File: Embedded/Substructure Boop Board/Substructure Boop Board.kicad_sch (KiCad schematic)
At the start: 1 part, among them U5 R FFC

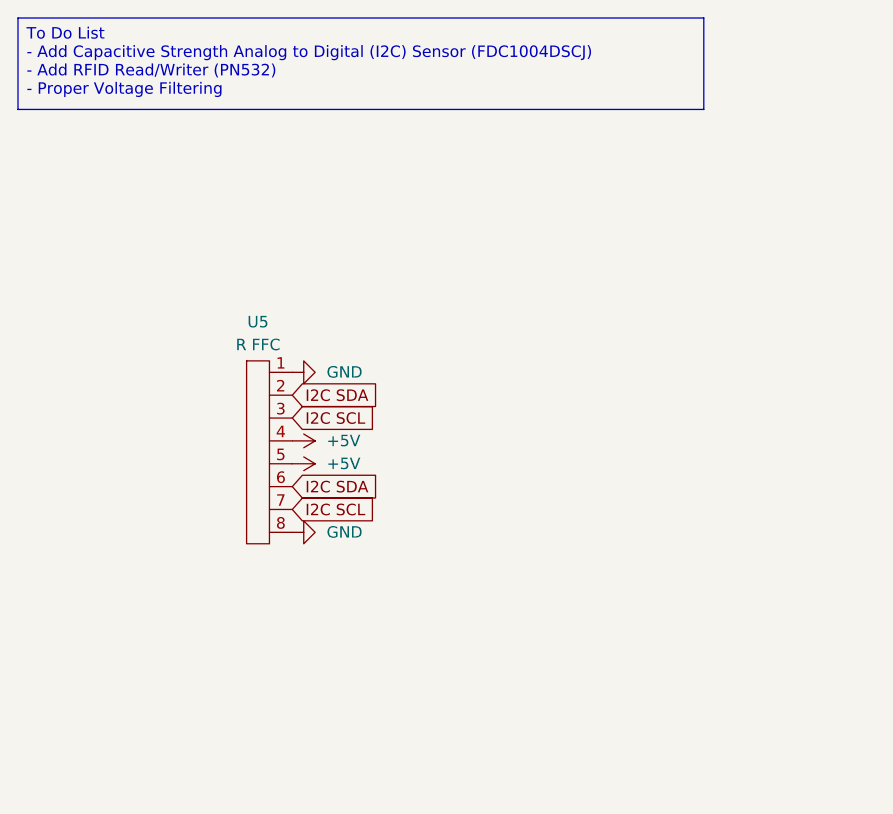
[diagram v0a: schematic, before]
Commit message: Added AD7142ACPZ-500RL7 IC to schematic
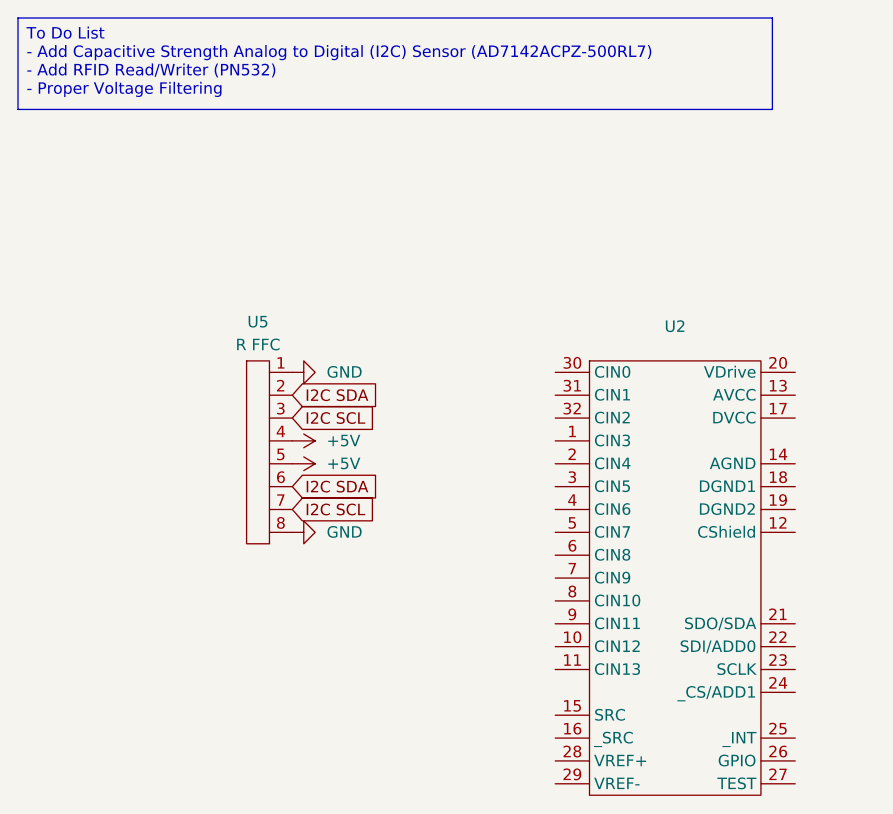
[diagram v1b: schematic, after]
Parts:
- added U2: ~, symbol AD7142ACPZ-500RL7:AD7142ACPZ-500RL7
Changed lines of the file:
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@@
 	(generator_version "9.0")
 	(paper "A4")
-	(text_box "To Do List\n- Add Capacitive Strength Analog to Digital (I2C) Sensor (FDC1004DSCJ)\n- Add RFID Read/Writer (PN532)\n- Proper Voltage Filtering"
+	(text_box "To Do List\n- Add Capacitive Strength Analog to Digital (I2C) Sensor (AD7142ACPZ-500RL7)\n- Add RFID Read/Writer (PN532)\n- Proper Voltage Filtering"
 		(exclude_from_sim no)
 		(at 25.4 25.4 0)
-		(size 76.2 10.16)
+		(size 83.82 10.16)
 		(margins 0.9525 0.9525 0.9525 0.9525)
 		(stroke
@@
 					(unit 1)
 				)
+			)
+		)
+	)
+	(symbol
+		(lib_id "AD7142ACPZ-500RL7:AD7142ACPZ-500RL7")
+		(at 88.9 63.5 0)
+		(unit 1)
+		(exclude_from_sim no)
+		(in_bom yes)
+		(on_board yes)
+		(dnp no)
+		(fields_autoplaced yes)
+		(property "Reference" "U2"
+			(at 98.425 59.69 0)
+			(effects
+				(font
+					(size 1.27 1.27)
+				)
+			)
+		)
+		(property "Value" "~"
+			(at 98.425 62.23 0)
+			(effects
+				(font
+					(size 1.27 1.27)
+				)
+			)
+		)
+		(property "Footprint" ""
+			(at 85.09 64.77 0)
+			(effects
+				(font
+					(size 1.27 1.27)
+				)
+				(hide yes)
+			)
+		)
+		(property "Datasheet" ""
+			(at 85.09 64.77 0)
+			(effects
+				(font
+					(size 1.27 1.27)
+				)
+				(hide yes)
+			)
+		)
+		(property "Description" ""
+			(at 85.09 64.77 0)
+			(effects
+				(font
+					(size 1.27 1.27)
+				)
+				(hide yes)
+			)
+		)
+		(pin "8"
+		)
+		(pin "15"
+		)
+		(pin "1"
+		)
+		(pin "5"
+		)
+		(pin "9"
+		)
+		(pin "11"
+		)
+		(pin "16"
+		)
+		(pin "12"
+		)
+		(pin "25"
+		)
+		(pin "30"
+		)
+		(pin "6"
+		)
+		(pin "14"
+		)
+		(pin "3"
+		)
+		(pin "4"
+		)
+		(pin "10"
+		)
+		(pin "32"
+		)
+		(pin "29"
+		)
+		(pin "19"
+		)
+		(pin "21"
+		)
+		(pin "7"
+		)
+		(pin "2"
+		)
+		(pin "31"
+		)
+		(pin "13"
+		)
+		(pin "28"
+		)
+		(pin "20"
+		)
+		(pin "17"
+		)
+		(pin "18"
+		)
+		(pin "22"
+		)
+		(pin "23"
+		)
+		(pin "24"
+		)
+		(pin "26"
+		)
+		(pin "27"
+		)
+		(instances
+			(project ""
+				(path "/6d158939-39e3-4f58-b43a-760f32d1166c"
+					(reference "U2")
+					(unit 1)
+				)

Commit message: Added Capacitive sensor driving circuitry
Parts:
- added C1: 10nF, Capacitor_SMD:C_0603_1608Metric_Pad1.08x0.95mm_HandSolder, symbol Device:C
- added C2: 10uF, Capacitor_SMD:C_0603_1608Metric_Pad1.08x0.95mm_HandSolder, symbol Device:C
- added C3: 0.1uF, Capacitor_SMD:C_0603_1608Metric_Pad1.08x0.95mm_HandSolder, symbol Device:C
- added R1, R2: 2.2K, Resistor_SMD:R_0603_1608Metric_Pad0.98x0.95mm_HandSolder, symbol Device:R
- U2: value ~ -> AD7142ACPZ-500RL7
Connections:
- net GND: now also U2.14 (AGND), U2.18 (DGND1), U2.19 (DGND2), U2.22 (SDI/ADD0), U2.24 (_CS/ADD1), U2.27 (TEST), U2.29 (VREF-), C1.1, C2.2, C3.2
- net I2C SCL: now also U2.23 (SCLK), R2.1
- net I2C SDA: now also U2.21 (SDO/SDA), R1.2
- net at U2.12 (CShield): now also C1.2
- net +3V3: now reaches U2.13 (AVCC)
- net +3V3: now also U2.17 (DVCC), U2.20 (VDrive), U2.28 (VREF+), C2.1, C3.1, R1.1, R2.2
- no-connect marks 0 -> 3

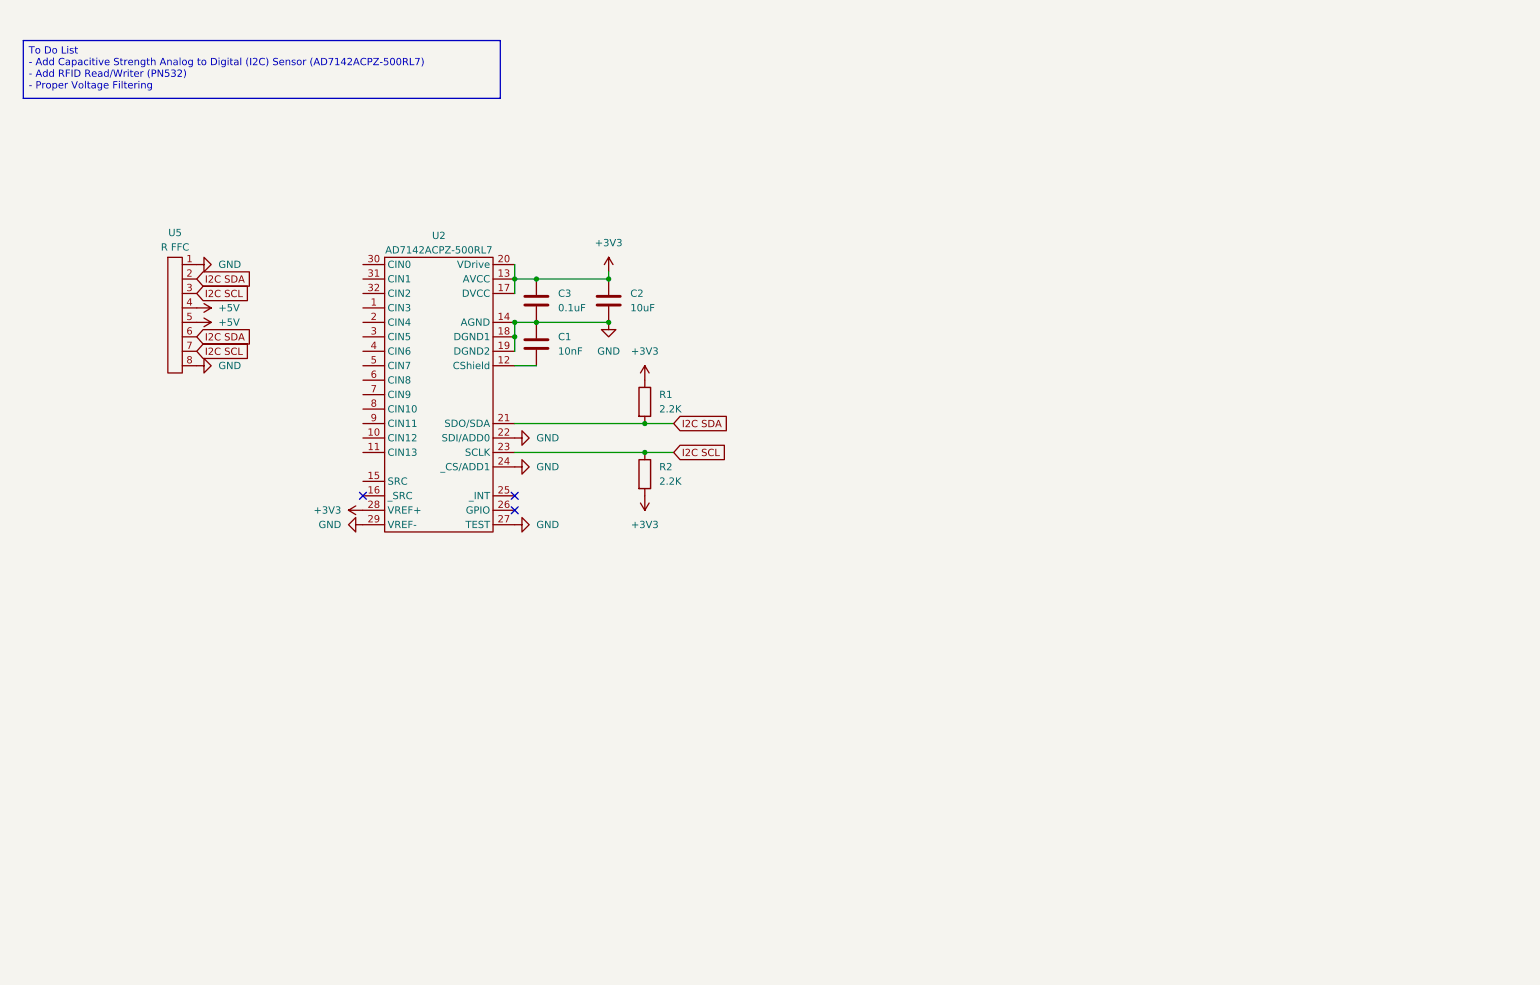
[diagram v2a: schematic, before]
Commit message: Added PN532 IC to schematic
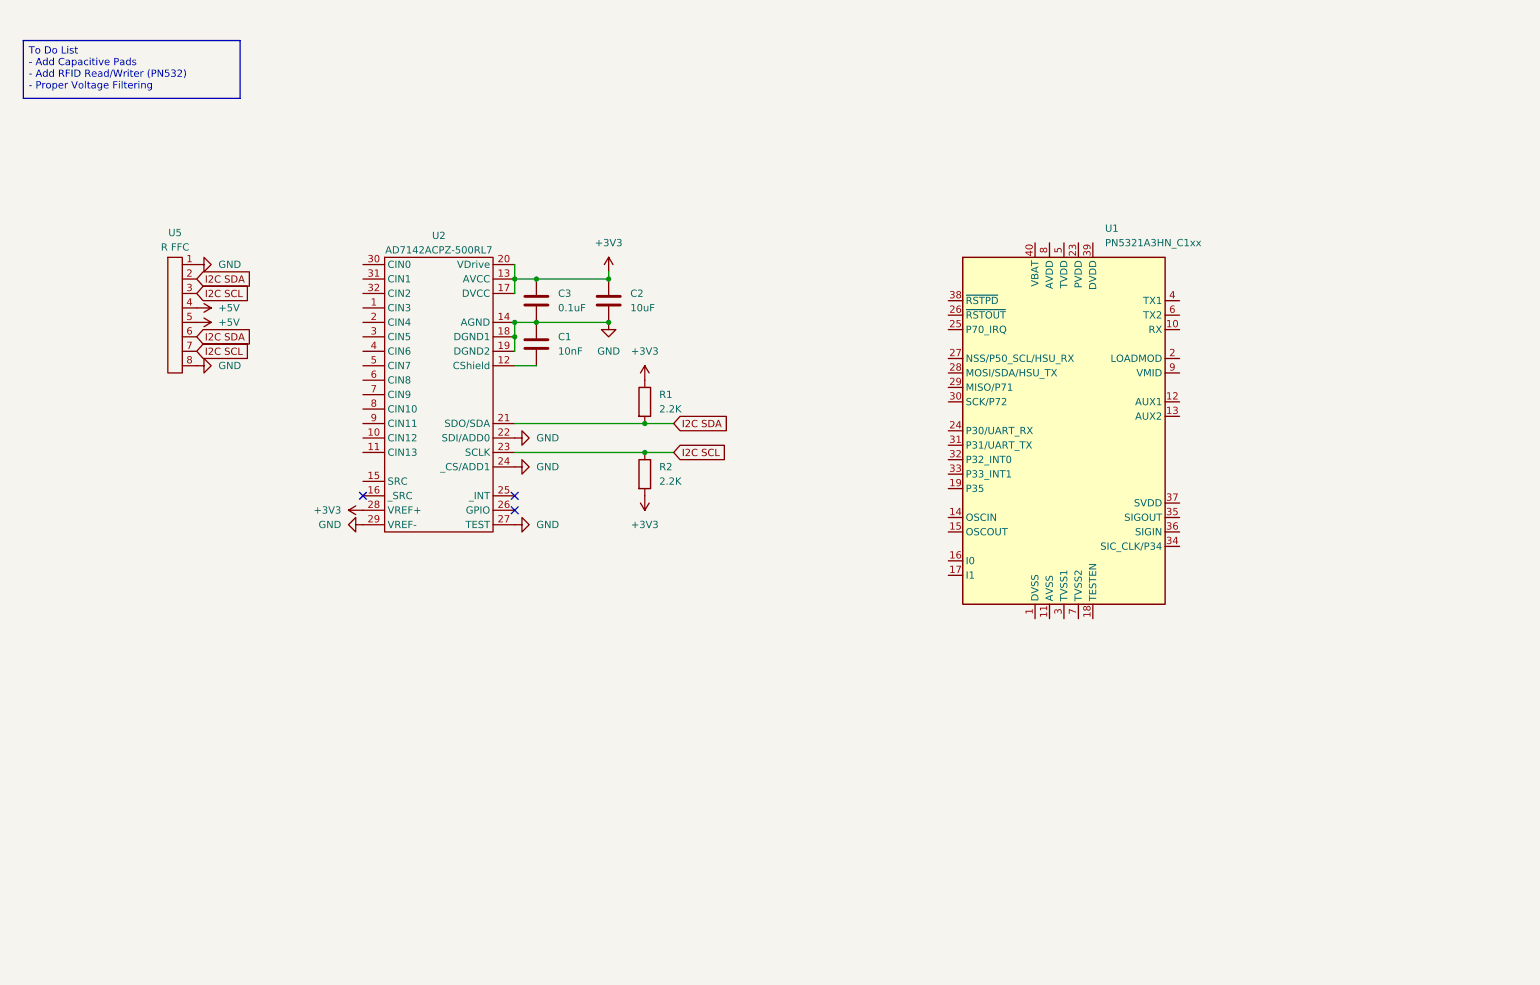
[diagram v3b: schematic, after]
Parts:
- added U1: PN5321A3HN_C1xx, Package_DFN_QFN:HVQFN-40-1EP_6x6mm_P0.5mm_EP4.1x4.1mm, symbol RF_NFC:PN5321A3HN_C1xx
- U2: footprint (none) -> Package_CSP:LFCSP-32-1EP_5x5mm_P0.5mm_EP3.1x3.1mm_ThermalVias
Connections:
- new net: U1.11 (AVSS), U1.41 (AVSS)
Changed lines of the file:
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@@
 	(generator_version "9.0")
 	(paper "A4")
-	(text_box "To Do List\n- Add Capacitive Strength Analog to Digital (I2C) Sensor (AD7142ACPZ-500RL7)\n- Add RFID Read/Writer (PN532)\n- Proper Voltage Filtering"
+	(text_box "To Do List\n- Add Capacitive Pads\n- Add RFID Read/Writer (PN532)\n- Proper Voltage Filtering"
 		(exclude_from_sim no)
 		(at 25.4 25.4 0)
-		(size 83.82 10.16)
+		(size 38.1 10.16)
 		(margins 0.9525 0.9525 0.9525 0.9525)
 		(stroke
@@
 			)
 		)
-		(property "Footprint" ""
+		(property "Footprint" "Package_CSP:LFCSP-32-1EP_5x5mm_P0.5mm_EP3.1x3.1mm_ThermalVias"
 			(at 85.09 64.77 0)
 			(effects
@@
 					(unit 1)
 				)
+			)
+		)
+	)
+	(symbol
+		(lib_id "RF_NFC:PN5321A3HN_C1xx")
+		(at 208.28 93.98 0)
+		(unit 1)
+		(exclude_from_sim no)
+		(in_bom yes)
+		(on_board yes)
+		(dnp no)
+		(fields_autoplaced yes)
+		(property "Reference" "U1"
+			(at 215.5033 58.42 0)
+			(effects
+				(font
+					(size 1.27 1.27)
+				)
+				(justify left)
+			)
+		)
+		(property "Value" "PN5321A3HN_C1xx"
+			(at 215.5033 60.96 0)
+			(effects
+				(font
+					(size 1.27 1.27)
+				)
+				(justify left)
+			)
+		)
+		(property "Footprint" "Package_DFN_QFN:HVQFN-40-1EP_6x6mm_P0.5mm_EP4.1x4.1mm"
+			(at 246.38 125.73 0)
+			(effects
+				(font
+					(size 1.27 1.27)
+				)
+				(hide yes)
+			)
+		)
+		(property "Datasheet" "https://www.nxp.com/docs/en/nxp/data-sheets/PN532_C1.pdf"
+			(at 208.28 88.9 0)
+			(effects
+				(font
+					(size 1.27 1.27)
+				)
+				(hide yes)
+			)
+		)
+		(property "Description" "Near Field Communication (NFC) controller, QFN-40"
+			(at 208.28 93.98 0)
+			(effects
+				(font
+					(size 1.27 1.27)
+				)
+				(hide yes)
+			)
+		)
+		(pin "7"
+		)
+		(pin "25"
+		)
+		(pin "24"
+		)
+		(pin "31"
+		)
+		(pin "33"
+		)
+		(pin "17"
+		)
+		(pin "40"
+		)
+		(pin "1"
+		)
+		(pin "26"
+		)
+		(pin "8"
+		)
+		(pin "41"
+		)
+		(pin "28"
+		)
+		(pin "19"
+		)
+		(pin "23"
+		)
+		(pin "5"
+		)
+		(pin "29"
+		)
+		(pin "30"
+		)
+		(pin "14"
+		)
+		(pin "32"
+		)
+		(pin "27"
+		)
+		(pin "15"
+		)
+		(pin "16"
+		)
+		(pin "11"
+		)
+		(pin "3"
+		)
+		(pin "38"
+		)
+		(pin "34"
+		)
+		(pin "18"
+		)
+		(pin "20"
+		)
+		(pin "13"
+		)
+		(pin "37"
+		)
+		(pin "39"
+		)
+		(pin "2"
+		)
+		(pin "6"
+		)
+		(pin "10"
+		)
+		(pin "9"
+		)
+		(pin "22"
+		)
+		(pin "4"
+		)
+		(pin "21"
+		)
+		(pin "12"
+		)
+		(pin "36"
+		)
+		(pin "35"
+		)
+		(instances
+			(project ""
+				(path "/6d158939-39e3-4f58-b43a-760f32d1166c"
+					(reference "U1")
+					(unit 1)
+				)

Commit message: Added RFID driving circuitry
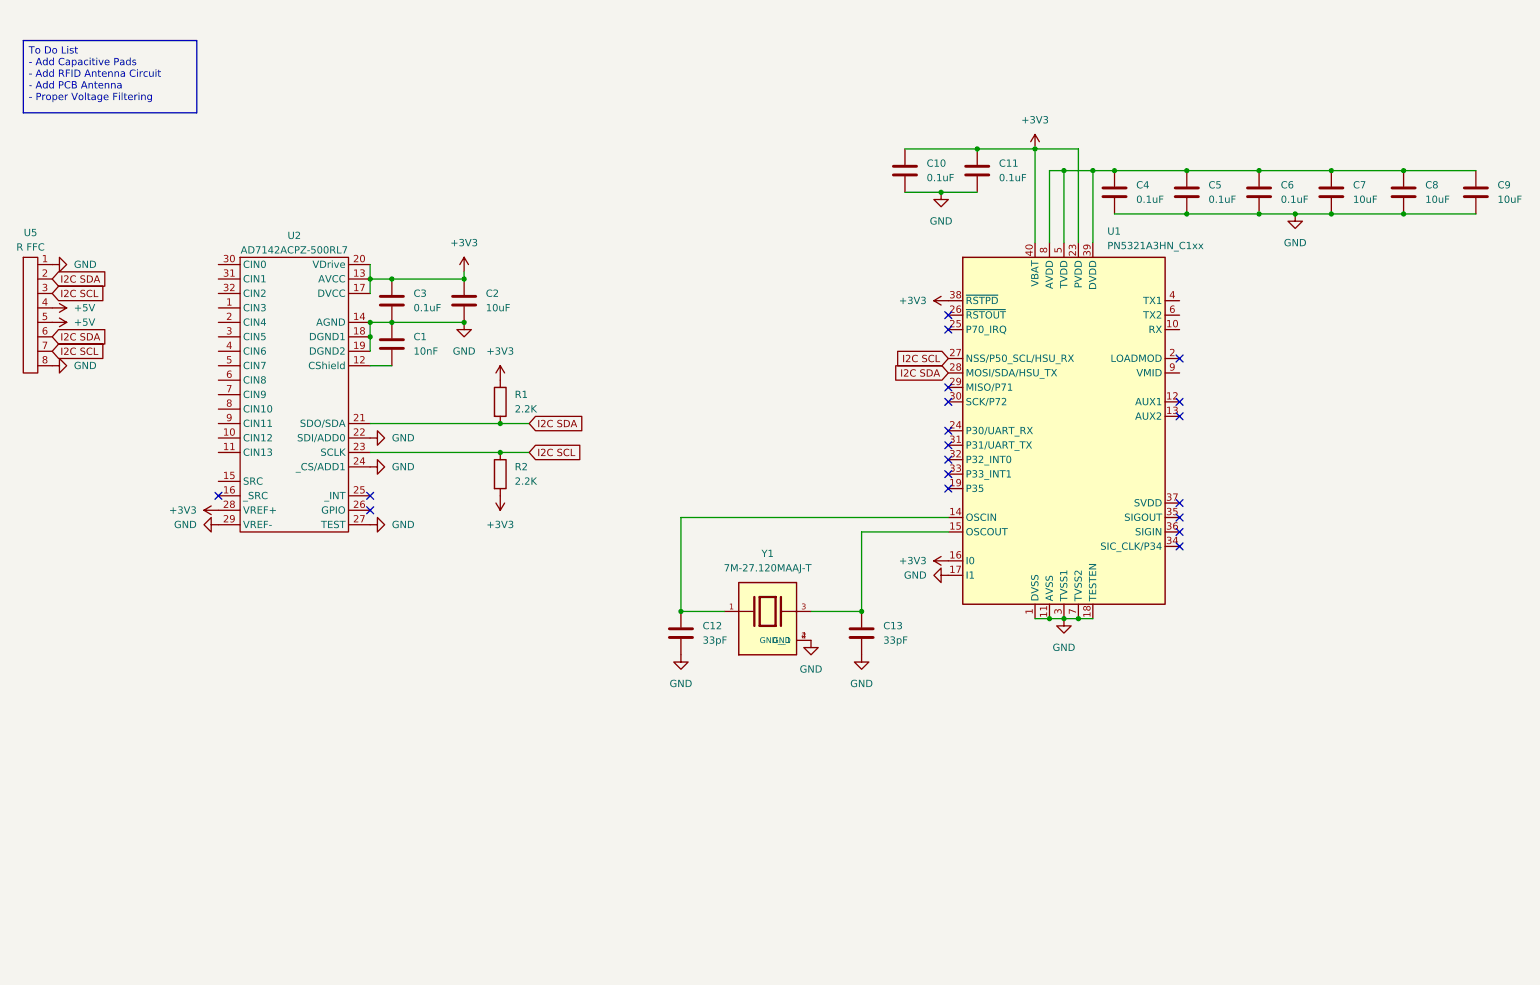
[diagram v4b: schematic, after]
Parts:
- added C10, C11, C4, C5, C6: 0.1uF, Capacitor_SMD:C_0603_1608Metric_Pad1.08x0.95mm_HandSolder, symbol Device:C
- added C12, C13: 33pF, Capacitor_SMD:C_0603_1608Metric_Pad1.08x0.95mm_HandSolder, symbol Device:C
- added C7, C8, C9: 10uF, Capacitor_SMD:C_0603_1608Metric_Pad1.08x0.95mm_HandSolder, symbol Device:C
- added Y1: 7M-27.120MAAJ-T, 7M-27.120MAAJ-T:XTAL_7M-27.120MAAJ-T, symbol 7M-27.120MAAJ-T:7M-27.120MAAJ-T
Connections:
- net +3V3: now also U1.16 (I0), U1.23 (PVDD), U1.38 (~{RSTPD}), U1.40 (VBAT), C10.1, C11.1
- net GND: now also U1.1 (DVSS), U1.11 (AVSS), U1.17 (I1), U1.18 (TESTEN), U1.3 (TVSS1), U1.41 (AVSS), U1.7 (TVSS2), C10.2, C11.2, C12.2, C13.2, C4.2, C5.2, C6.2, C7.2, C8.2, C9.2, Y1.2 (GND), Y1.4 (GND__1)
- net I2C SCL: now also U1.27 (NSS/P50_SCL/HSU_RX)
- net I2C SDA: now also U1.28 (MOSI/SDA/HSU_TX)
- net at U1.14 (OSCIN): now also C12.1, Y1.1
- net at U1.15 (OSCOUT): now also C13.1, Y1.3
- net at U1.39 (DVDD): now also U1.5 (TVDD), U1.8 (AVDD), C4.1, C5.1, C6.1, C7.1, C8.1, C9.1
- no-connect marks 3 -> 19
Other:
- moved on the sheet: C1, C2, C3, R1, R2, U2, U5

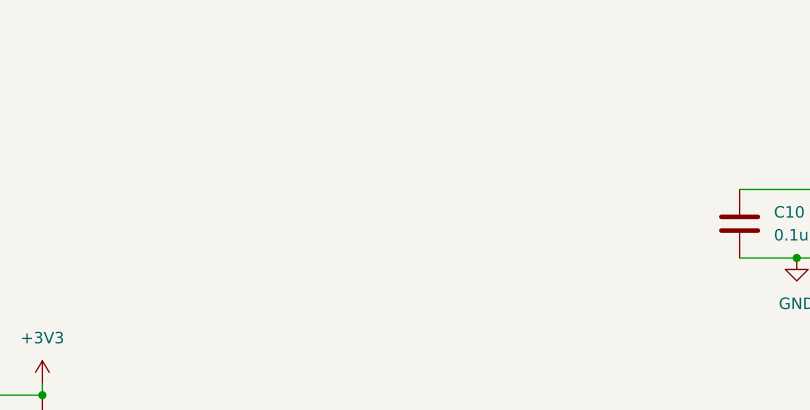
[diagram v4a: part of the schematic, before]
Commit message: Added 3V3 LDO
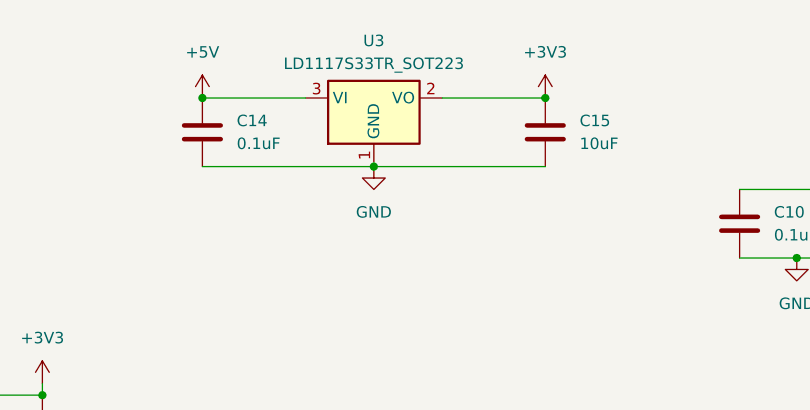
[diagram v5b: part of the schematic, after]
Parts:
- added C14: 0.1uF, Capacitor_SMD:C_0603_1608Metric_Pad1.08x0.95mm_HandSolder, symbol Device:C
- added C15: 10uF, Capacitor_SMD:C_0603_1608Metric_Pad1.08x0.95mm_HandSolder, symbol Device:C
- added U3: LD1117S33TR_SOT223, Package_TO_SOT_SMD:SOT-223-3_TabPin2, symbol Regulator_Linear:LD1117S33TR_SOT223
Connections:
- net +3V3: now also C15.1, U3.2 (VO)
- net +5V: now also C14.1, U3.3 (VI)
- net GND: now also C14.2, C15.2, U3.1 (GND)
